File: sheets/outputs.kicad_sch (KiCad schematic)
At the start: 10 parts, among them U20 ULN2803A

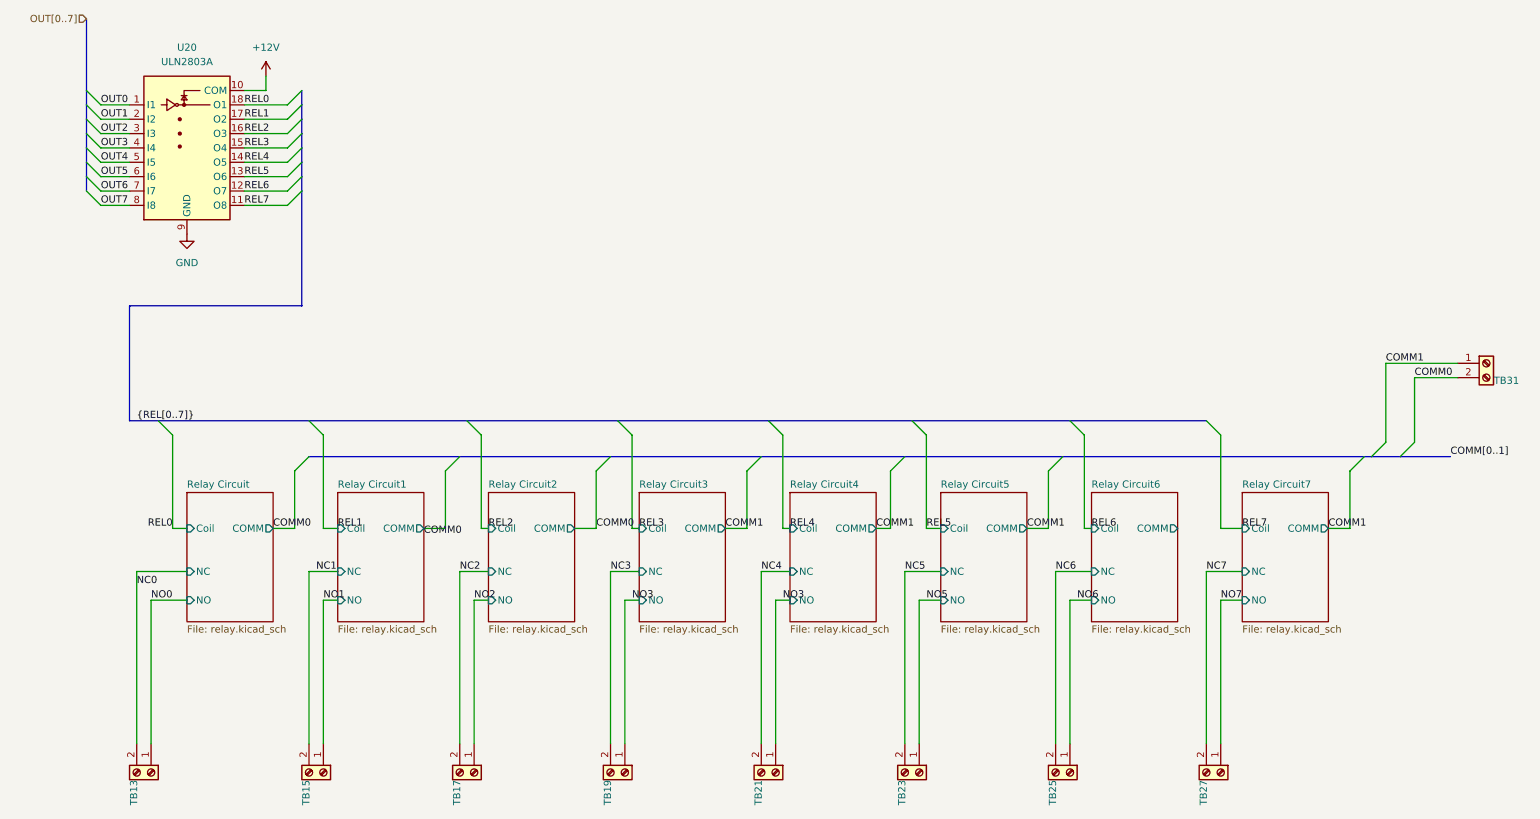
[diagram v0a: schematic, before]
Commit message: finished routing SPI, I2C and MikroBUS
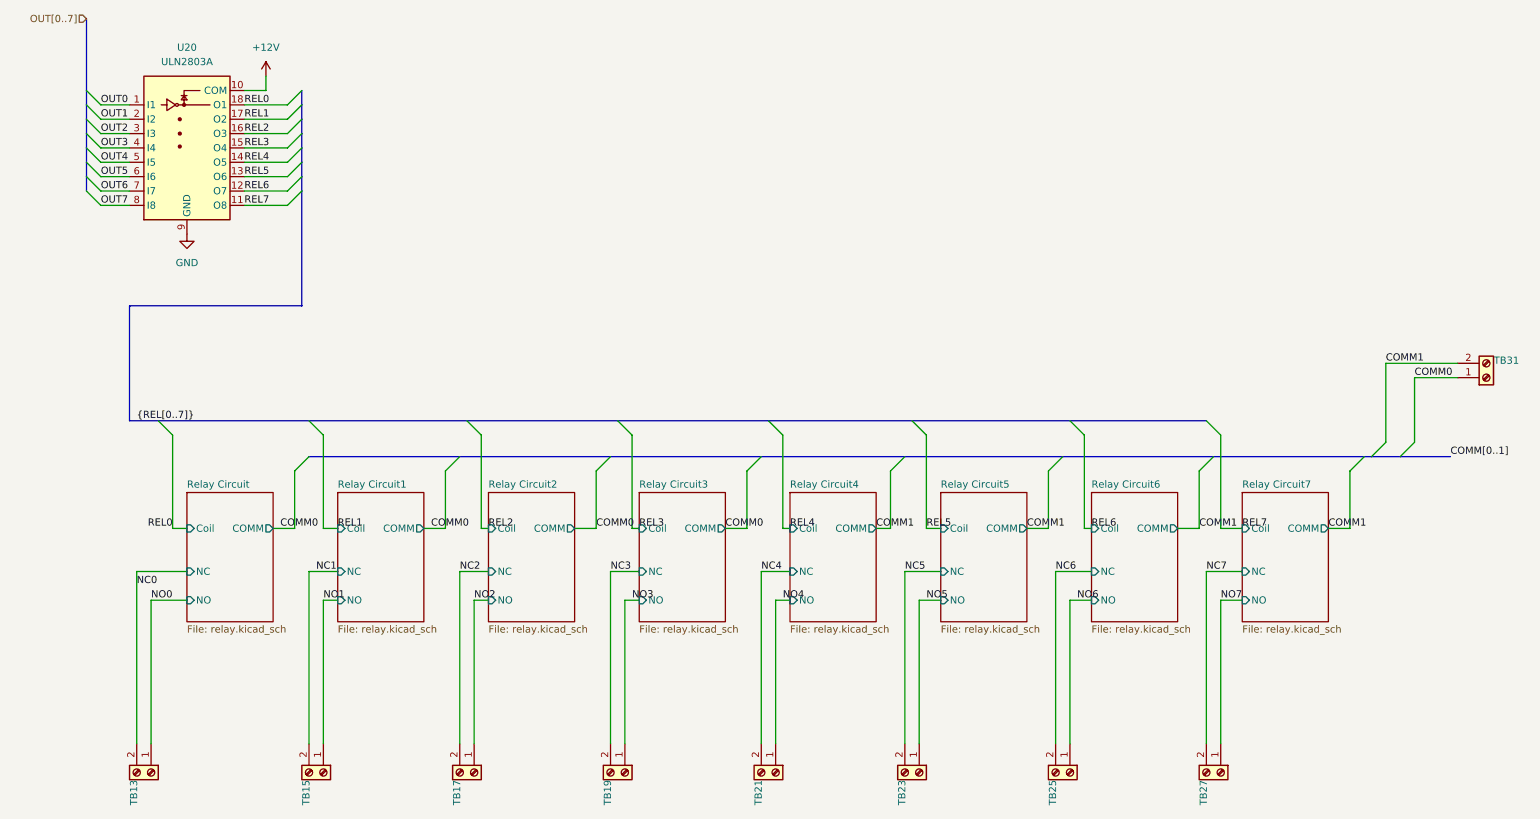
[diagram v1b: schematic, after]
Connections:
- net COMM0: now also TB31.1 (Pin_1); no longer TB31.2 (Pin_2)
- net COMM1: now also TB31.2 (Pin_2); no longer TB31.1 (Pin_1)
- net NO3: no longer TB21.1 (Pin_1)
- new net NO4: TB21.1 (Pin_1)
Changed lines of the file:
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@@
+		)
+	)
+	(bus_entry
+		(at 224.79 93.98)
+		(size -2.54 2.54)
+		(stroke
+			(width 0)
+			(type default)
 		)
 	)
@@
 		)
 	)
+	(wire
+		(pts
+			(xy 222.25 96.52) (xy 222.25 106.68)
+		)
+		(stroke
+			(width 0)
+			(type default)
+		)
+	)
 	(bus
 		(pts
@@
 	(bus
 		(pts
-			(xy 198.12 93.98) (xy 251.46 93.98)
+			(xy 224.79 93.98) (xy 251.46 93.98)
+		)
+		(stroke
+			(width 0)
+			(type default)
+		)
+	)
+	(bus
+		(pts
+			(xy 198.12 93.98) (xy 224.79 93.98)
 		)
 		(stroke
@@
 	(wire
 		(pts
+			(xy 58.42 106.68) (xy 62.23 106.68)
+		)
+		(stroke
+			(width 0)
+			(type default)
+		)
+	)
+	(wire
+		(pts
 			(xy 167.64 96.52) (xy 167.64 106.68)
 		)
@@
 		)
 	)
+	(wire
+		(pts
+			(xy 85.09 106.68) (xy 88.9 106.68)
+		)
+		(stroke
+			(width 0)
+			(type default)
+		)
+	)
 	(bus
 		(pts
@@
 	(wire
 		(pts
-			(xy 88.9 106.68) (xy 85.09 106.68)
-		)
-		(stroke
-			(width 0)
-			(type default)
-		)
-	)
-	(wire
-		(pts
 			(xy 53.34 34.29) (xy 60.96 34.29)
 		)
@@
 		)
 	)
+	(wire
+		(pts
+			(xy 218.44 106.68) (xy 222.25 106.68)
+		)
+		(stroke
+			(width 0)
+			(type default)
+		)
+	)
 	(bus
 		(pts
@@
 		(pts
 			(xy 36.83 119.38) (xy 43.18 119.38)
-		)
-		(stroke
-			(width 0)
-			(type default)
-		)
-	)
-	(wire
-		(pts
-			(xy 62.23 106.68) (xy 58.42 106.68)
 		)
 		(stroke
@@
 	)
 	(label "COMM0"
-		(at 58.42 106.68 0)
+		(at 59.69 106.68 0)
 		(effects
 			(font
@@
 		)
 	)
-	(label "NO3"
+	(label "NO4"
 		(at 148.59 119.38 0)
 		(effects
@@
 		)
 	)
-	(label "COMM1"
+	(label "COMM0"
 		(at 138.43 106.68 0)
 		(effects
@@
 		)
 	)
+	(label "COMM1"
+		(at 222.25 106.68 0)
+		(effects
+			(font
+				(size 1.27 1.27)
+			)
+			(justify left bottom)
+		)
+	)
 	(label "REL5"
 		(at 53.34 44.45 0)
@@
 	)
 	(label "COMM0"
-		(at 85.09 107.95 0)
+		(at 86.36 106.68 0)
 		(effects
 			(font
@@
 	(symbol
 		(lib_id "Connector:Screw_Terminal_01x02")
-		(at 273.05 77.47 0)
+		(at 273.05 80.01 0)
+		(mirror x)
 		(unit 1)
 		(exclude_from_sim no)
@@
 		(dnp no)
 		(property "Reference" "TB31"
-			(at 276.606 80.518 0)
+			(at 276.606 76.962 0)
 			(effects
 				(font
@@
 		)
 		(property "Value" "MKDSN 1,5/ 2-5,08"
-			(at 273.05 83.82 0)
+			(at 273.05 73.66 0)
 			(effects
 				(font
@@
 		)
 		(property "Footprint" "TerminalBlock_Phoenix:TerminalBlock_Phoenix_MKDS-1,5-2-5.08_1x02_P5.08mm_Horizontal"
-			(at 273.05 77.47 0)
+			(at 273.05 80.01 0)
 			(effects
 				(font
@@
 		)
 		(property "Datasheet" "~"
-			(at 273.05 77.47 0)
+			(at 273.05 80.01 0)
 			(effects
 				(font
@@
 		)
 		(property "Description" "Generic screw terminal, single row, 01x02, script generated (kicad-library-utils/schlib/autogen/connector/)"
-			(at 273.05 77.47 0)
+			(at 273.05 80.01 0)
 			(effects
 				(font
@@
 		)
 		(property "Partnumber" "  MKDSN 1,5/ 2-5,08 "
-			(at 273.05 77.47 0)
+			(at 273.05 80.01 0)
 			(effects
 				(font
@@
 		)
 		(property "LCSC" "C5183989"
-			(at 273.05 77.47 0)
+			(at 273.05 80.01 0)
 			(effects
 				(font
@@
 		)
 		(property "Manufacturer" "Phoenix Contact"
-			(at 273.05 77.47 0)
-			(effects
-				(font
+			(at 273.05 80.01 0)
+			(effects
+				(font
